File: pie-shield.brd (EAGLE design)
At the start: 35.5 x 56.2 mm, 15 parts, among them IC6 78L05, IC8 MAX487, X6 RJ45-8L-B

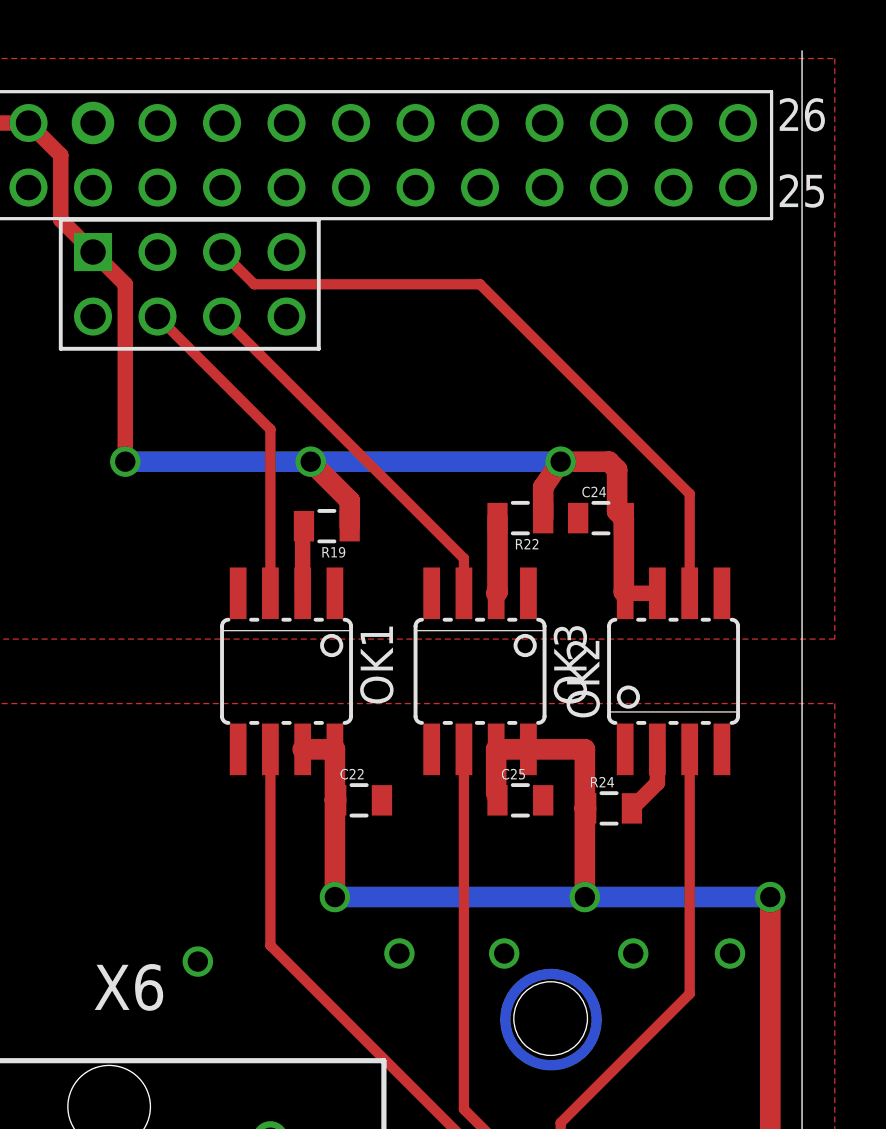
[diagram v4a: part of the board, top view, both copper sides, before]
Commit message: rewired to use uart txd, rxd and rts
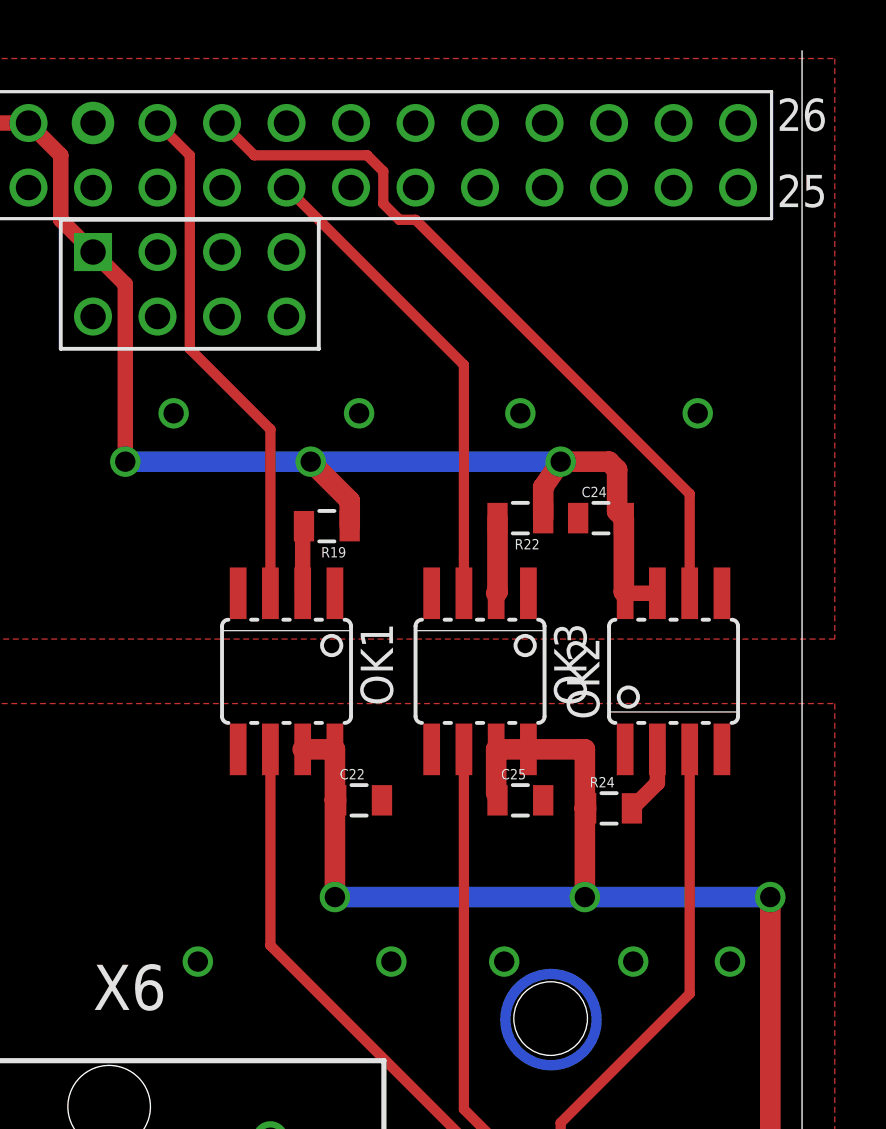
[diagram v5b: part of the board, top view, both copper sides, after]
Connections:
- net RXD_AL: now also U$2.P1_10; no longer U$2.P5_5
- net SELECT: now also U$2.P1_11; no longer U$2.P5_6
- net TXD_AL: now also U$2.P1_8; no longer U$2.P5_4
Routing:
- net TXD_AL: track 12.7 -> 20.4 mm
- net SELECT: track 14.8 -> 18.9 mm
- net RXD_AL: track 26.3 -> 29.1 mm
- net +5V: vias 3 -> 7
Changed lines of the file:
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@@
 </polygon>
 <via x="11.7475" y="20.32" extent="1-16" drill="0.8" shape="octagon"/>
-<via x="19.685" y="20.6375" extent="1-16" drill="0.8" shape="octagon"/>
-<via x="23.8125" y="20.6375" extent="1-16" drill="0.8" shape="octagon"/>
-<via x="28.8925" y="20.6375" extent="1-16" drill="0.8" shape="octagon"/>
-<via x="32.7025" y="20.6375" extent="1-16" drill="0.8" shape="octagon"/>
+<via x="19.3675" y="20.32" extent="1-16" drill="0.8" shape="octagon"/>
+<via x="23.8125" y="20.32" extent="1-16" drill="0.8" shape="octagon"/>
+<via x="28.8925" y="20.32" extent="1-16" drill="0.8" shape="octagon"/>
+<via x="32.7025" y="20.32" extent="1-16" drill="0.8" shape="octagon"/>
 </signal>
 <signal name="A1">
@@
 <signal name="RXD_AL">
 <contactref element="OK2" pad="6"/>
-<contactref element="U$2" pad="P5_5"/>
-<wire x1="12.7" y1="48.26" x2="13.97" y2="46.99" width="0.4064" layer="1"/>
-<wire x1="13.97" y1="46.99" x2="22.86" y2="46.99" width="0.4064" layer="1"/>
-<wire x1="22.86" y1="46.99" x2="31.115" y2="38.735" width="0.4064" layer="1"/>
+<wire x1="20.32" y1="49.53" x2="31.115" y2="38.735" width="0.4064" layer="1"/>
 <wire x1="31.115" y1="38.735" x2="31.115" y2="34.8234" width="0.4064" layer="1"/>
+<contactref element="U$2" pad="P1_10"/>
+<wire x1="13.97" y1="52.07" x2="12.7" y2="53.34" width="0.4064" layer="1"/>
+<wire x1="13.97" y1="52.07" x2="18.415" y2="52.07" width="0.4064" layer="1"/>
+<wire x1="18.415" y1="52.07" x2="19.05" y2="51.435" width="0.4064" layer="1"/>
+<wire x1="19.05" y1="51.435" x2="19.05" y2="50.165" width="0.4064" layer="1"/>
+<wire x1="19.05" y1="50.165" x2="19.685" y2="49.53" width="0.4064" layer="1"/>
+<wire x1="19.685" y1="49.53" x2="20.32" y2="49.53" width="0.4064" layer="1"/>
 </signal>
 <signal name="TXD_AL">
 <contactref element="OK1" pad="3"/>
-<contactref element="U$2" pad="P5_4"/>
-<wire x1="10.16" y1="45.72" x2="14.605" y2="41.275" width="0.4064" layer="1"/>
 <wire x1="14.605" y1="41.275" x2="14.605" y2="34.8234" width="0.4064" layer="1"/>
+<contactref element="U$2" pad="P1_8"/>
+<wire x1="10.16" y1="53.34" x2="11.43" y2="52.07" width="0.4064" layer="1"/>
+<wire x1="11.43" y1="52.07" x2="11.43" y2="44.45" width="0.4064" layer="1"/>
+<wire x1="11.43" y1="44.45" x2="14.605" y2="41.275" width="0.4064" layer="1"/>
 </signal>
 <signal name="N$37">
@@
 <wire x1="28.5225" y1="37.7825" x2="28.5225" y2="34.8759" width="0.8128" layer="1"/>
 <wire x1="28.5225" y1="34.8759" x2="28.575" y2="34.8234" width="0.8128" layer="1"/>
+<via x="10.795" y="41.91" extent="1-16" drill="0.8" shape="octagon"/>
+<via x="18.0975" y="41.91" extent="1-16" drill="0.8" shape="octagon"/>
+<via x="24.4475" y="41.91" extent="1-16" drill="0.8" shape="octagon"/>
+<via x="31.4325" y="41.91" extent="1-16" drill="0.8" shape="octagon"/>
 </signal>
 <signal name="SELECT">
 <contactref element="OK3" pad="3"/>
-<contactref element="U$2" pad="P5_6"/>
-<wire x1="12.7" y1="45.72" x2="22.225" y2="36.195" width="0.4064" layer="1"/>
-<wire x1="22.225" y1="36.195" x2="22.225" y2="34.8234" width="0.4064" layer="1"/>
+<wire x1="22.225" y1="36.195" x2="22.225" y2="35.56" width="0.4064" layer="1"/>
+<contactref element="U$2" pad="P1_11"/>
+<wire x1="22.225" y1="35.56" x2="22.225" y2="34.8234" width="0.4064" layer="1"/>
+<wire x1="15.24" y1="50.8" x2="22.225" y2="43.815" width="0.4064" layer="1"/>
+<wire x1="22.225" y1="43.815" x2="22.225" y2="36.195" width="0.4064" layer="1"/>
 </signal>
 <signal name="GND">

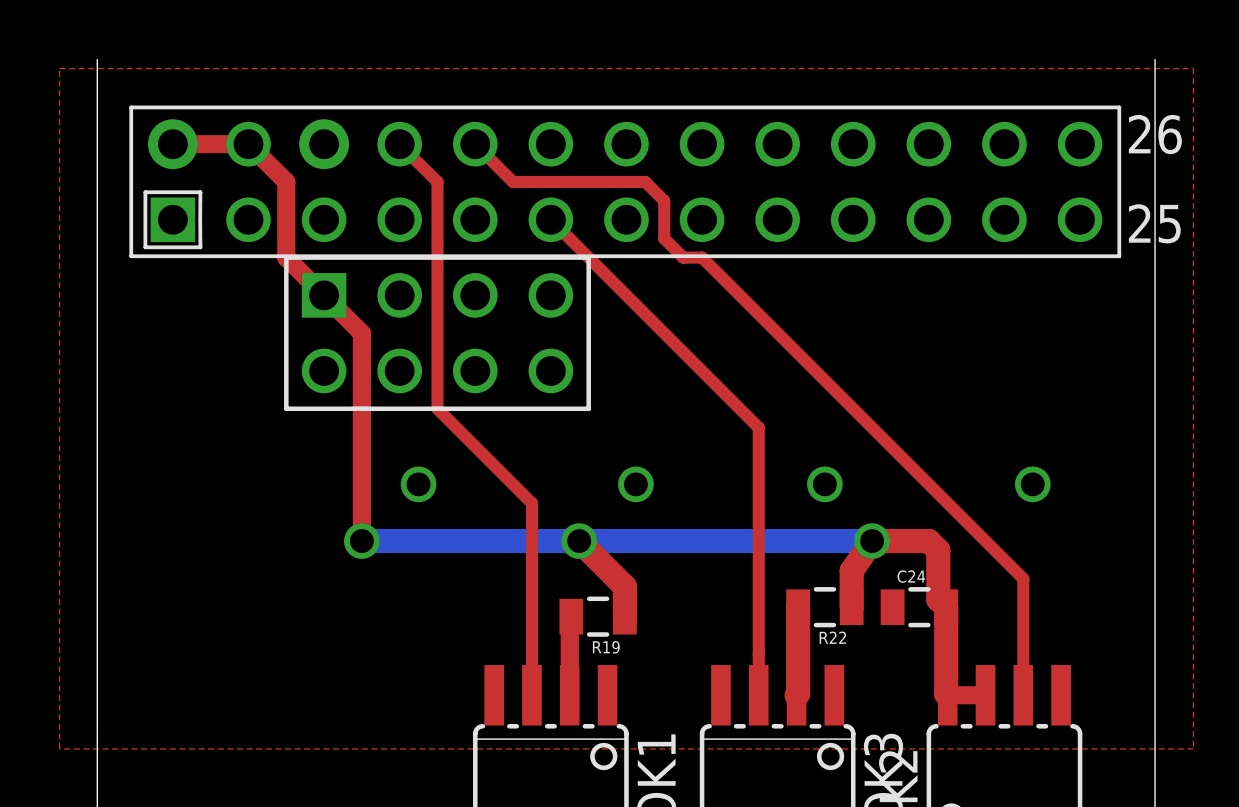
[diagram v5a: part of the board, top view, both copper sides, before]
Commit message: set optocouplers on pie side to 3.3V levels
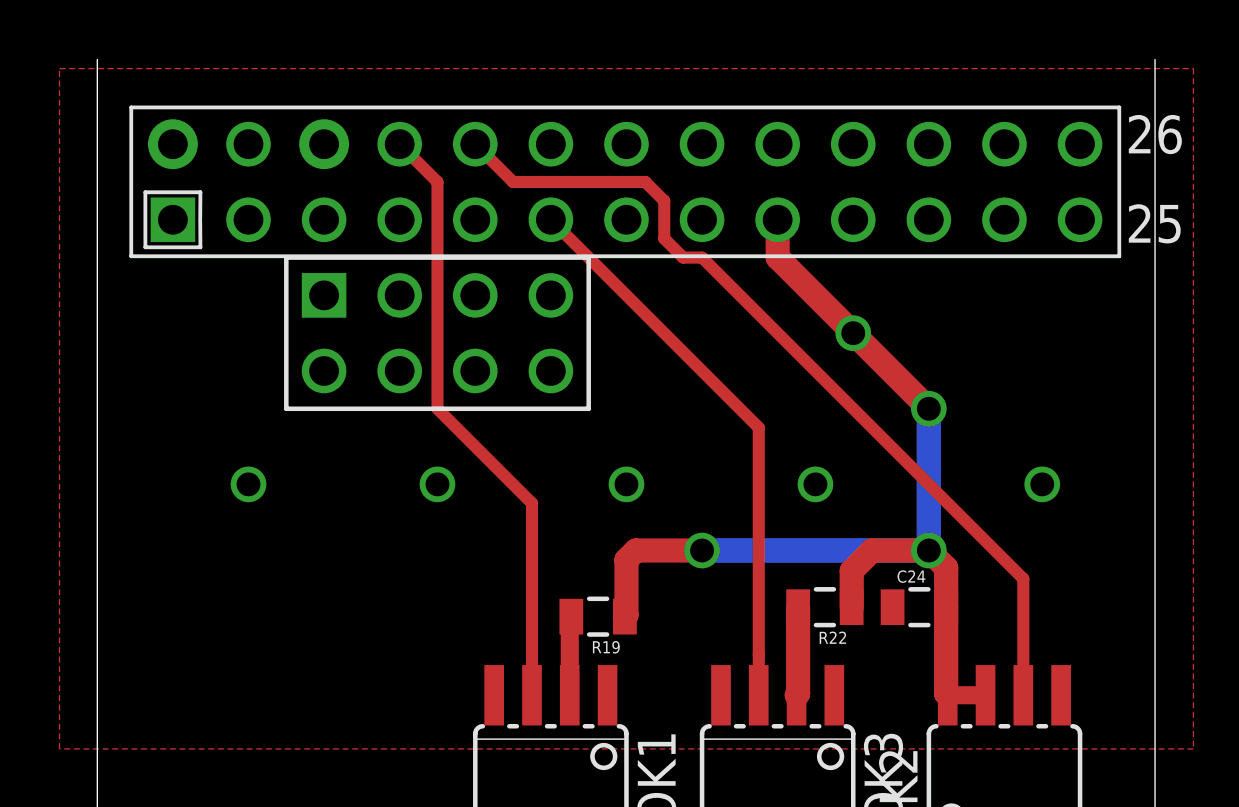
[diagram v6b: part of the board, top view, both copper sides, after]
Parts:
- OK2: value HCPL0601 -> FOD060L
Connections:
- new net +3.3V: C24.2, OK2.7, OK2.8, R19.1, R22.1, U$2.P1_1, U$2.P1_17, U$2.P5_2
- net +5V: no longer C24.2, OK2.7, OK2.8, R19.1, R22.1
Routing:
- net +5V: track 48.8 -> 0.00 mm, vias 7 -> 0
- net +3.3V: track 0.00 -> 35.9 mm, vias 0 -> 4
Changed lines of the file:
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@@
 <attribute name="OC_FARNELL" value="9995102" x="-45.72" y="96.52" size="1.778" layer="27" rot="R180" display="off"/>
 </element>
-<element name="OK2" library="optocoupler" package="SOIC08" value="HCPL0601" x="30.48" y="31.75">
+<element name="OK2" library="optocoupler" package="SOIC08" value="FOD060L" x="30.48" y="31.75">
 <attribute name="OC_NEWARK" value="88H7776" x="101.6" y="-33.02" size="1.778" layer="27" display="off"/>
 <attribute name="MPN" value="HCPL-0601-000E" x="101.6" y="-33.02" size="1.778" layer="27" display="off"/>
@@
 </signal>
 <signal name="+5V">
-<contactref element="OK2" pad="8"/>
-<contactref element="C24" pad="2"/>
-<contactref element="OK2" pad="7"/>
-<contactref element="R22" pad="1"/>
-<contactref element="R19" pad="1"/>
 <contactref element="U$2" pad="P1_2"/>
 <contactref element="U$2" pad="P1_4"/>
 <contactref element="U$2" pad="P5_1"/>
-<wire x1="2.54" y1="53.34" x2="5.08" y2="53.34" width="0.6096" layer="1"/>
-<wire x1="5.08" y1="53.34" x2="6.35" y2="52.07" width="0.6096" layer="1"/>
-<wire x1="6.35" y1="52.07" x2="6.35" y2="49.53" width="0.6096" layer="1"/>
-<wire x1="6.35" y1="49.53" x2="7.62" y2="48.26" width="0.6096" layer="1"/>
-<wire x1="7.62" y1="48.26" x2="8.89" y2="46.99" width="0.6096" layer="1"/>
-<via x="26.035" y="40.005" extent="1-16" drill="0.8" shape="octagon"/>
-<wire x1="28.575" y1="34.8234" x2="29.845" y2="34.8234" width="0.6096" layer="1"/>
-<wire x1="16.1925" y1="40.005" x2="26.035" y2="40.005" width="0.8128" layer="16"/>
-<via x="16.1925" y="40.005" extent="1-16" drill="0.8" shape="octagon"/>
-<wire x1="8.89" y1="46.99" x2="8.89" y2="40.005" width="0.6096" layer="1"/>
-<via x="8.89" y="40.005" extent="1-16" drill="0.8" shape="octagon"/>
-<wire x1="8.89" y1="40.005" x2="16.1925" y2="40.005" width="0.8128" layer="16"/>
-<wire x1="16.1925" y1="40.005" x2="17.7275" y2="38.47" width="0.8128" layer="1"/>
-<wire x1="17.7275" y1="38.47" x2="17.7275" y2="37.465" width="0.8128" layer="1"/>
-<wire x1="26.035" y1="40.005" x2="25.3475" y2="39" width="0.8128" layer="1"/>
-<wire x1="25.3475" y1="39" x2="25.3475" y2="37.7825" width="0.8128" layer="1"/>
-<wire x1="26.035" y1="40.005" x2="27.94" y2="40.005" width="0.8128" layer="1"/>
-<wire x1="27.94" y1="40.005" x2="28.2575" y2="39.6875" width="0.8128" layer="1"/>
-<wire x1="28.2575" y1="39.6875" x2="28.2575" y2="38.0475" width="0.8128" layer="1"/>
-<wire x1="28.2575" y1="38.0475" x2="28.5225" y2="37.7825" width="0.8128" layer="1"/>
-<wire x1="28.5225" y1="37.7825" x2="28.5225" y2="34.8759" width="0.8128" layer="1"/>
-<wire x1="28.5225" y1="34.8759" x2="28.575" y2="34.8234" width="0.8128" layer="1"/>
-<via x="10.795" y="41.91" extent="1-16" drill="0.8" shape="octagon"/>
-<via x="18.0975" y="41.91" extent="1-16" drill="0.8" shape="octagon"/>
-<via x="24.4475" y="41.91" extent="1-16" drill="0.8" shape="octagon"/>
-<via x="31.4325" y="41.91" extent="1-16" drill="0.8" shape="octagon"/>
+<wire x1="2.54" y1="53.34" x2="5.08" y2="53.34" width="0" layer="19" extent="1-1"/>
+<wire x1="7.62" y1="48.26" x2="5.08" y2="53.34" width="0" layer="19" extent="1-1"/>
 </signal>
 <signal name="SELECT">
@@
 <contactref element="U$2" pad="P5_7"/>
 <contactref element="U$2" pad="P1_6"/>
+<via x="5.08" y="41.91" extent="1-16" drill="0.8" shape="octagon"/>
+<via x="11.43" y="41.91" extent="1-16" drill="0.8" shape="octagon"/>
+<via x="17.78" y="41.91" extent="1-16" drill="0.8" shape="octagon"/>
+<via x="24.13" y="41.91" extent="1-16" drill="0.8" shape="octagon"/>
+<via x="31.75" y="41.91" extent="1-16" drill="0.8" shape="octagon"/>
+</signal>
+<signal name="+3.3V">
+<contactref element="OK2" pad="8"/>
+<contactref element="C24" pad="2"/>
+<contactref element="OK2" pad="7"/>
+<wire x1="28.575" y1="34.8234" x2="29.845" y2="34.8234" width="0.6096" layer="1"/>
+<wire x1="28.5225" y1="37.7825" x2="28.5225" y2="34.8759" width="0.8128" layer="1"/>
+<wire x1="28.5225" y1="34.8759" x2="28.575" y2="34.8234" width="0.8128" layer="1"/>
+<contactref element="U$2" pad="P1_1"/>
+<contactref element="U$2" pad="P1_17"/>
+<contactref element="U$2" pad="P5_2"/>
+<wire x1="22.86" y1="50.8" x2="22.86" y2="49.53" width="0.8128" layer="1"/>
+<wire x1="22.86" y1="49.53" x2="27.94" y2="44.45" width="0.8128" layer="1"/>
+<via x="27.94" y="44.45" extent="1-16" drill="0.8" shape="octagon"/>
+<wire x1="27.94" y1="44.45" x2="27.94" y2="39.6875" width="0.8128" layer="16"/>
+<via x="27.94" y="39.6875" extent="1-16" drill="0.8" shape="octagon"/>
+<wire x1="27.94" y1="39.6875" x2="28.5225" y2="39.105" width="0.8128" layer="1"/>
+<wire x1="28.5225" y1="39.105" x2="28.5225" y2="37.7825" width="0.8128" layer="1"/>
+<contactref element="R22" pad="1"/>
+<contactref element="R19" pad="1"/>
+<via x="20.32" y="39.6875" extent="1-16" drill="0.8" shape="octagon"/>
+<wire x1="25.3475" y1="37.7825" x2="25.3475" y2="39" width="0.8128" layer="1"/>
+<wire x1="25.3475" y1="39" x2="26.035" y2="39.6875" width="0.8128" layer="1"/>
+<wire x1="26.035" y1="39.6875" x2="27.94" y2="39.6875" width="0.8128" layer="1"/>
+<wire x1="20.32" y1="39.6875" x2="27.94" y2="39.6875" width="0.8128" layer="16"/>
+<wire x1="20.32" y1="39.6875" x2="18.0975" y2="39.6875" width="0.8128" layer="1"/>
+<wire x1="18.0975" y1="39.6875" x2="17.78" y2="39.37" width="0.8128" layer="1"/>
+<wire x1="17.78" y1="39.37" x2="17.78" y2="37.5175" width="0.8128" layer="1"/>
+<wire x1="17.78" y1="37.5175" x2="17.7275" y2="37.465" width="0.8128" layer="1"/>
+<wire x1="7.62" y1="45.72" x2="2.54" y2="50.8" width="0" layer="19" extent="1-1"/>
+<wire x1="17.78" y1="39.37" x2="7.62" y2="45.72" width="0" layer="19" extent="1-1"/>
+<via x="25.4" y="46.99" extent="1-16" drill="0.8" shape="octagon"/>
 </signal>
 </signals>
-<errors>
-</errors>
 </board>
 </drawing>
